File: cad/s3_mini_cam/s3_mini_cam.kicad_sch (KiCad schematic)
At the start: 58 parts, among them U1 SFV24R-3STBE1HLF, U2 USB3090-30-A, U3 2pin_header, U4 2pin_header, U5 ESP32-S3-WROOM-1-N8R2, U6 TPS62A02APDDCR, U7 TPS62A02APDDCR, U8 TPS62A02APDDCR, U9 4pin_header

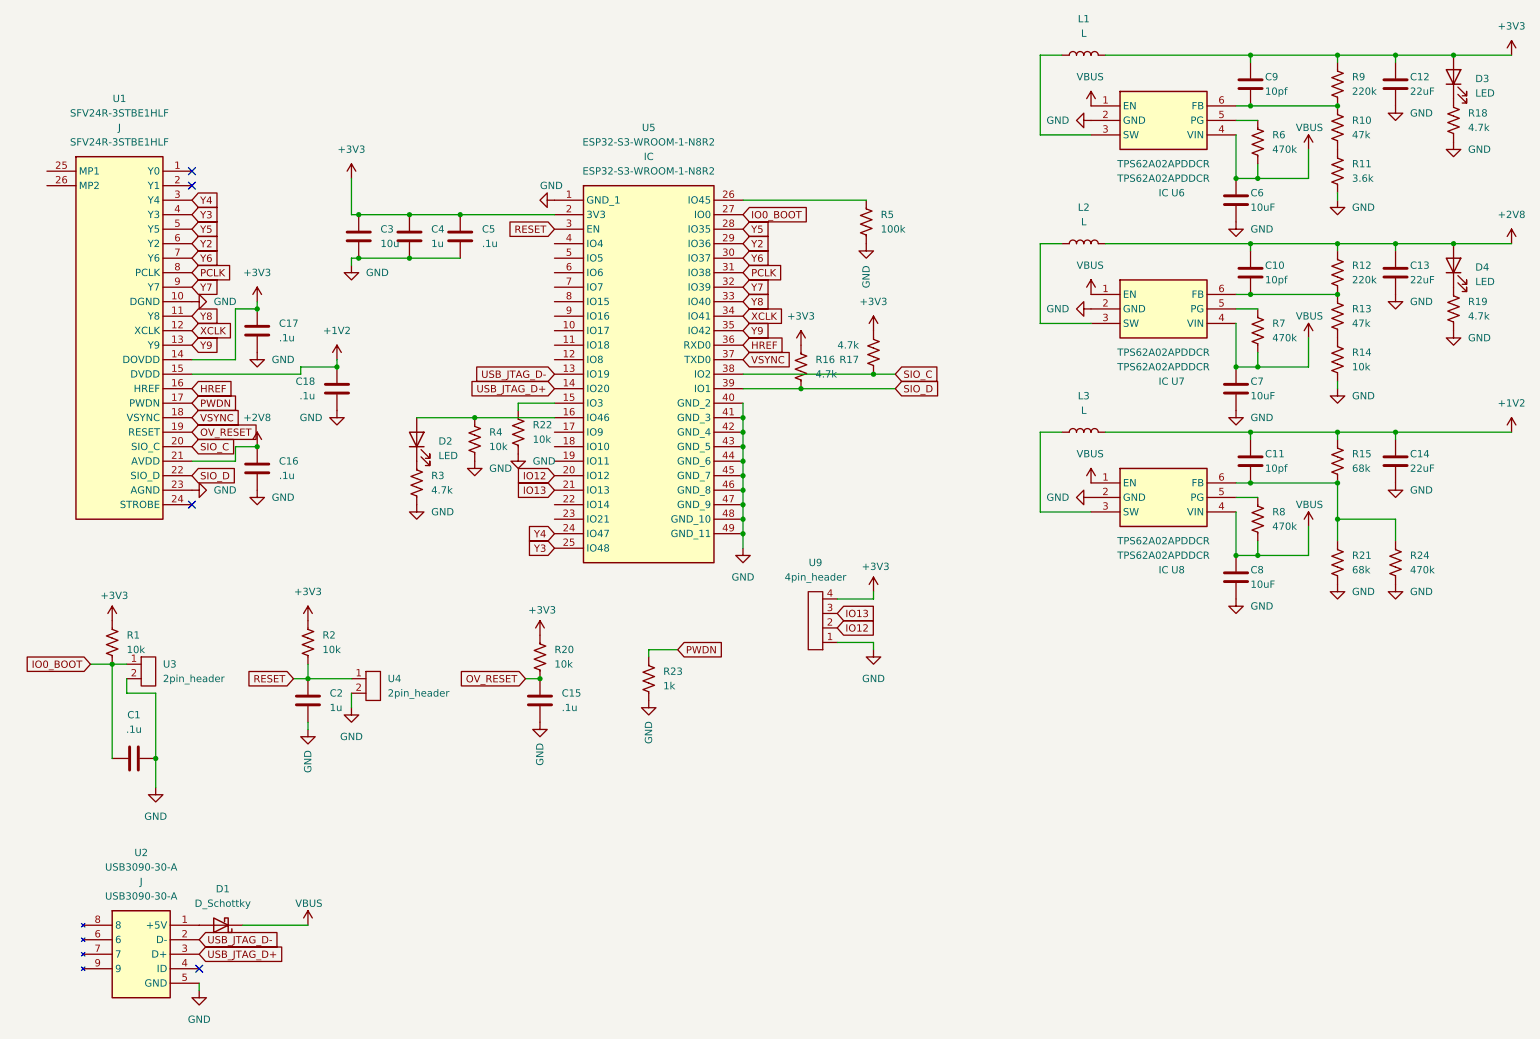
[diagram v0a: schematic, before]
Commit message: Added s3cam pcbs
Signed-off-by: Andrew Wock <ajwock@gmail.com>
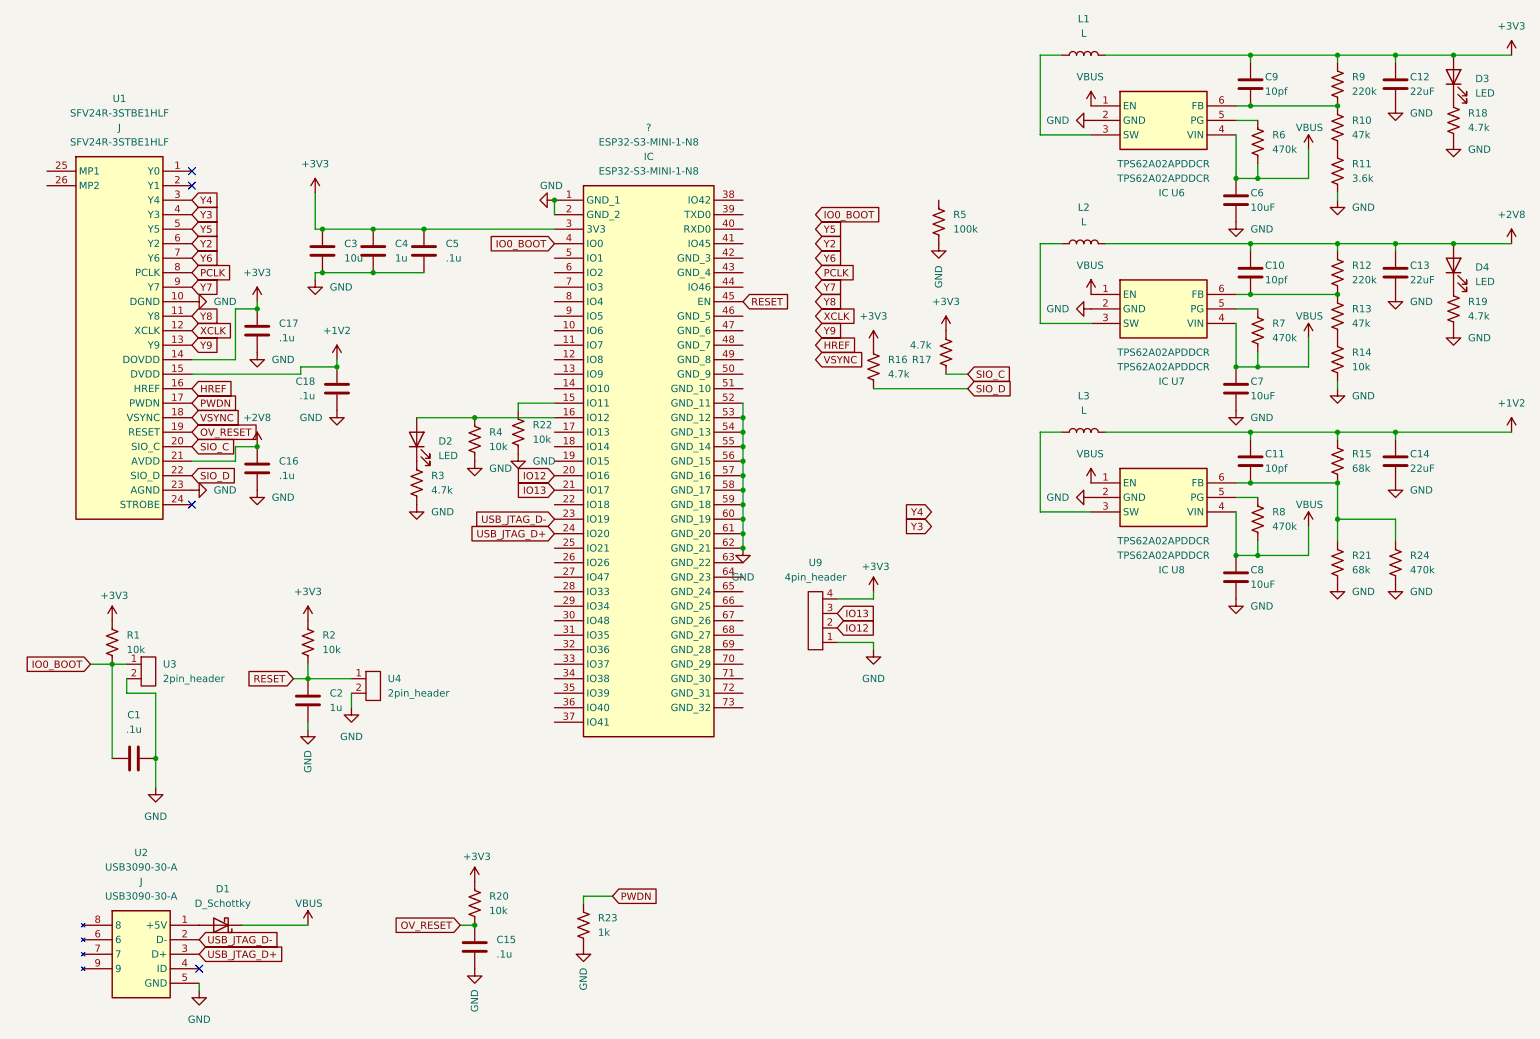
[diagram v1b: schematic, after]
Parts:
- removed U5: ESP32-S3-WROOM-1-N8R2, Imported:ESP32S3WROOM1N8R2, symbol ESP32-S3-WROOM-1-N8R2:ESP32-S3-WROOM-1-N8R2
- added ?: ESP32-S3-MINI-1-N8, symbol ESP32-S3-MINI-1-N8:ESP32-S3-MINI-1-N8
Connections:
- net +3V3: now also ?.3 (3V3)
- net GND: now also ?.1 (GND_1), ?.2 (GND_2), ?.52 (GND_11), ?.53 (GND_12), ?.54 (GND_13), ?.55 (GND_14), ?.56 (GND_15), ?.57 (GND_16), ?.58 (GND_17), ?.59 (GND_18), ?.60 (GND_19), ?.61 (GND_20), ?.62 (GND_21)
- net IO0_BOOT: now also ?.4 (IO0)
- net IO12: now also ?.20 (IO16)
- net IO13: now also ?.21 (IO17)
- net RESET: now also ?.45 (EN)
- net USB_JTAG_D+: now also ?.24 (IO20)
- net USB_JTAG_D-: now also ?.23 (IO19)
- net at R22.1: now also ?.15 (IO11)
- net at D2.2 (A), R4.1: now also ?.16 (IO12)
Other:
- moved on the sheet: C15, C3, C4, C5, R16, R17, R20, R23, R5
